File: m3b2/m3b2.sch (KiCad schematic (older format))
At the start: 41 parts, among them P6 MicroD-37Pins, Q1 MD3251, Q2 MD3251, U1 MC307, U10 MC308, U11 MC306, U12 MC308, U13 MC308, U14 MC308, U15 MC306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

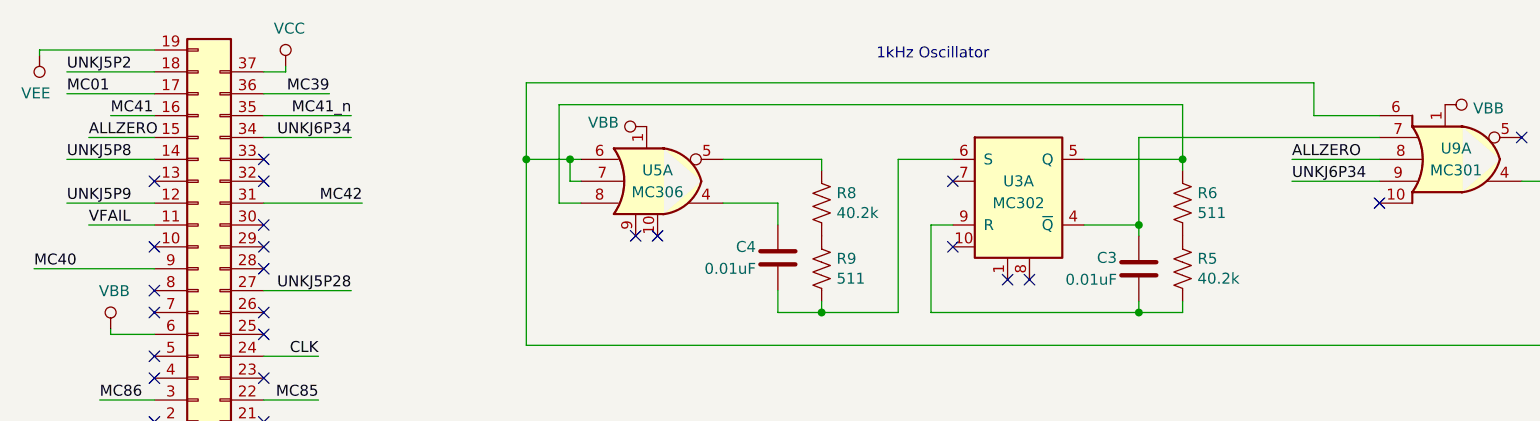
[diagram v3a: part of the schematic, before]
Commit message: Initial schematic for module 4, board 1, plus lots of associated net name updates. The shift register is done, but a lot of surrounding NOR logic still needs to be untangled.
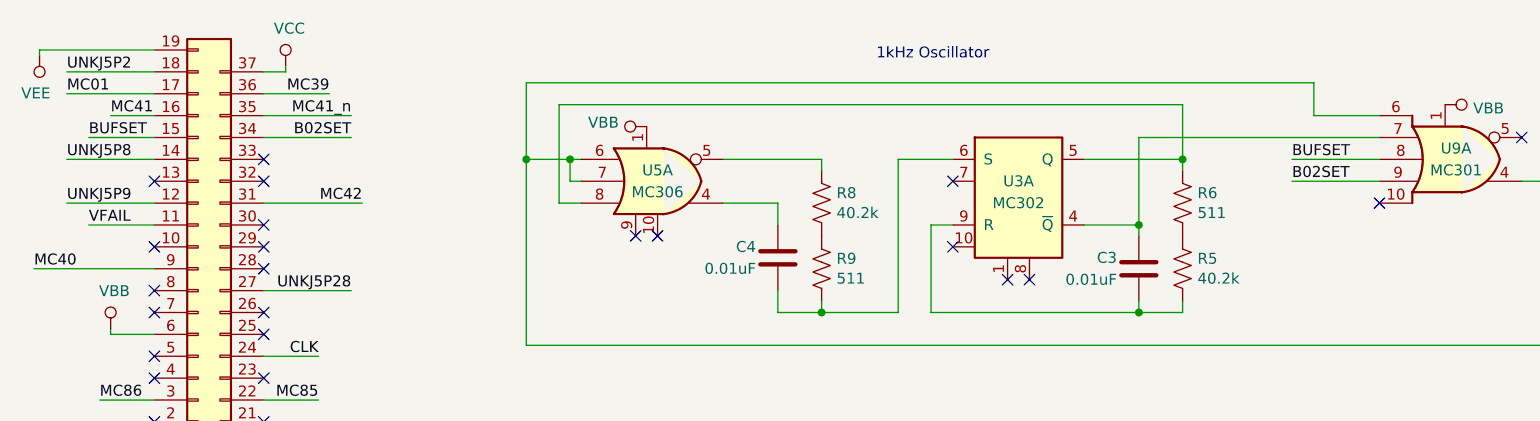
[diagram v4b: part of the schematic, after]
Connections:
- net ALLZERO renamed BUFSET
- net UNKJ6P34 renamed B02SET
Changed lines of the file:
@@
 	1200 1150 900  1150
 Text Label 900  1150 0    50   ~ 0
-ALLZERO
+BUFSET
 Wire Wire Line
 	1700 1850 2100 1850
@@
 	1700 1150 2100 1150
 Text Label 2100 1150 2    50   ~ 0
-UNKJ6P34
+B02SET
 Wire Wire Line
 	1700 1050 2100 1050
@@
 	6800 1250 6400 1250
 Text Label 6400 1250 0    50   ~ 0
-ALLZERO
+BUFSET
 Wire Wire Line
 	6800 1350 6400 1350
 Text Label 6400 1350 0    50   ~ 0
-UNKJ6P34
+B02SET
 Wire Wire Line
 	7450 1350 7700 1350

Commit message: Some work on reorganizing the module 3 schematics
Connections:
- net at U13.4 (~Q), U5.6, U5.7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: now also U10.1 (R), U14.1 (R), U4.1 (R), U6.1 (R)
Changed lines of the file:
@@
 	9050 6400 8350 6400
 Wire Wire Line
-	9050 2100 9050 6400
+	9050 2100 9050 3800
 $Comp
 L Device:R_US R12
@@
 Text Label 8450 9100 2    50   ~ 0
 MC42
+Wire Wire Line
+	4550 3800 9050 3800
+Connection ~ 4550 3800
+Connection ~ 9050 3800
+Wire Wire Line
+	9050 3800 9050 6400
 $EndSCHEMATC

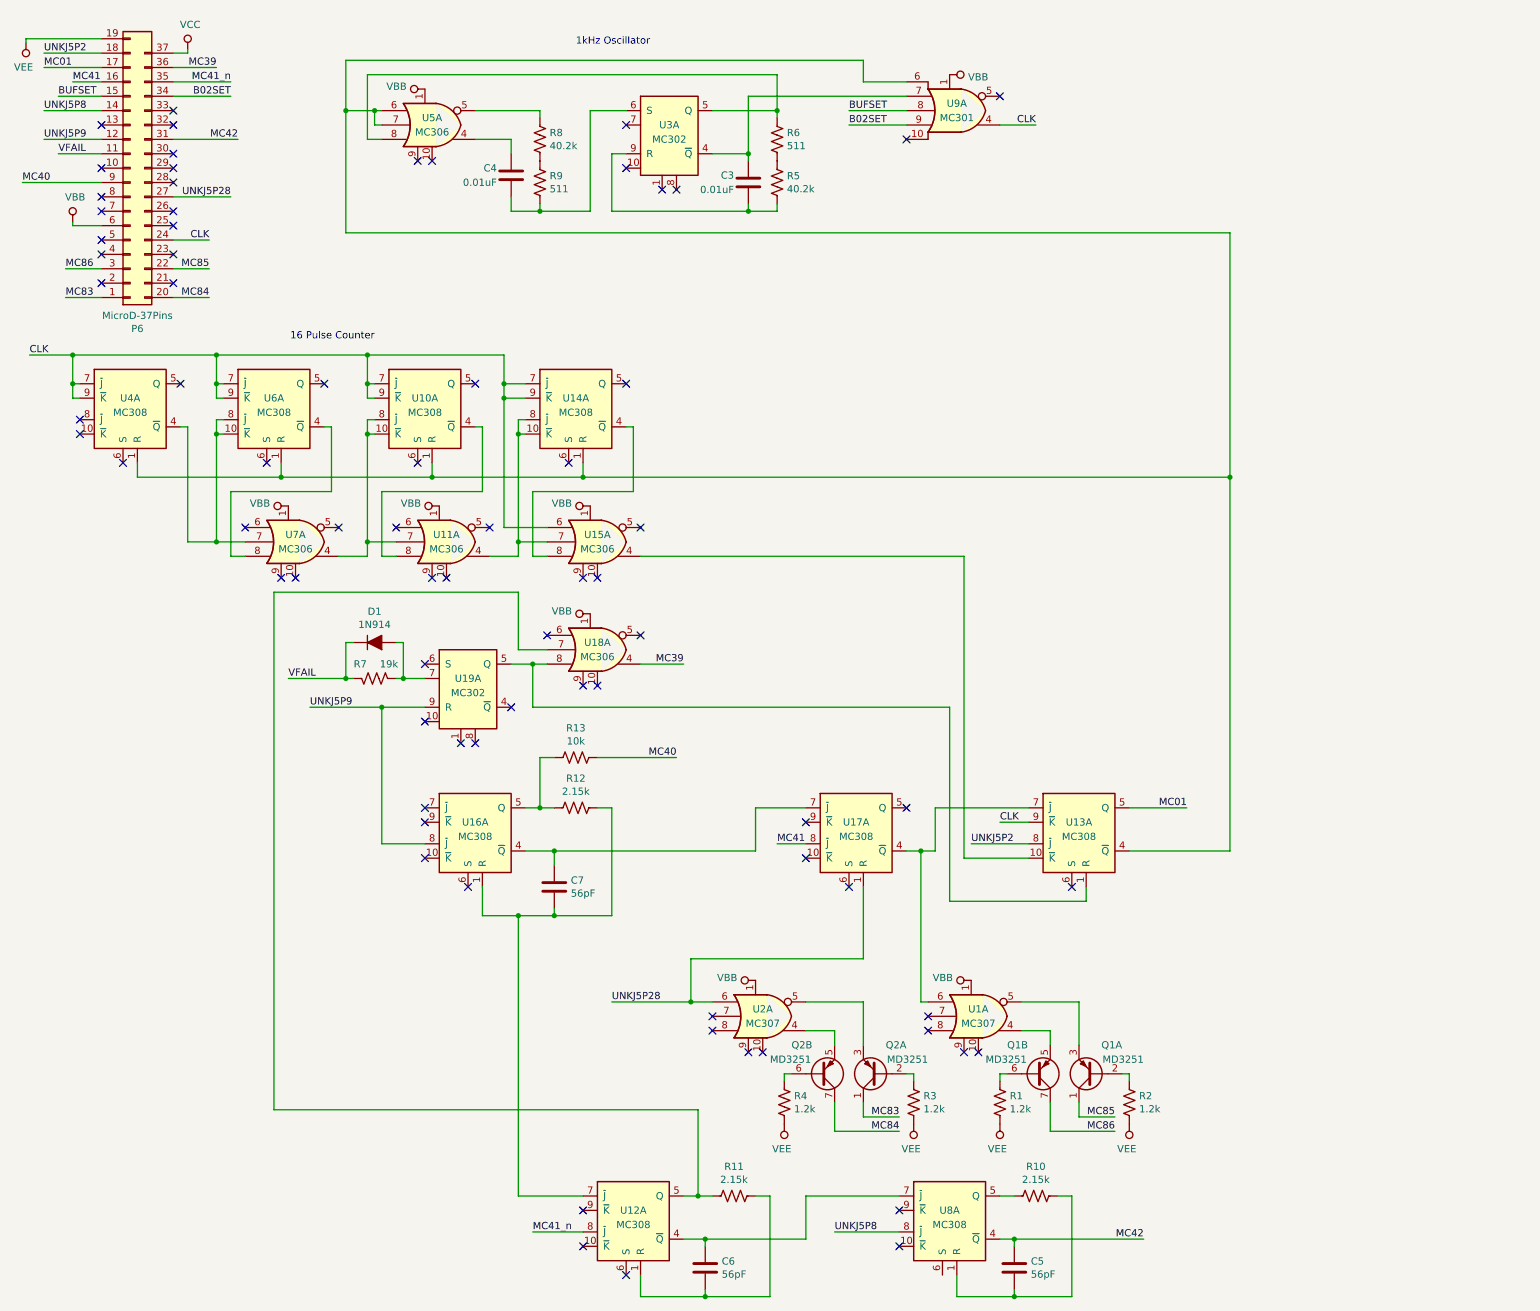
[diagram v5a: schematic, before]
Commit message: Finished untangling the module 3 schematics and gave every net a name
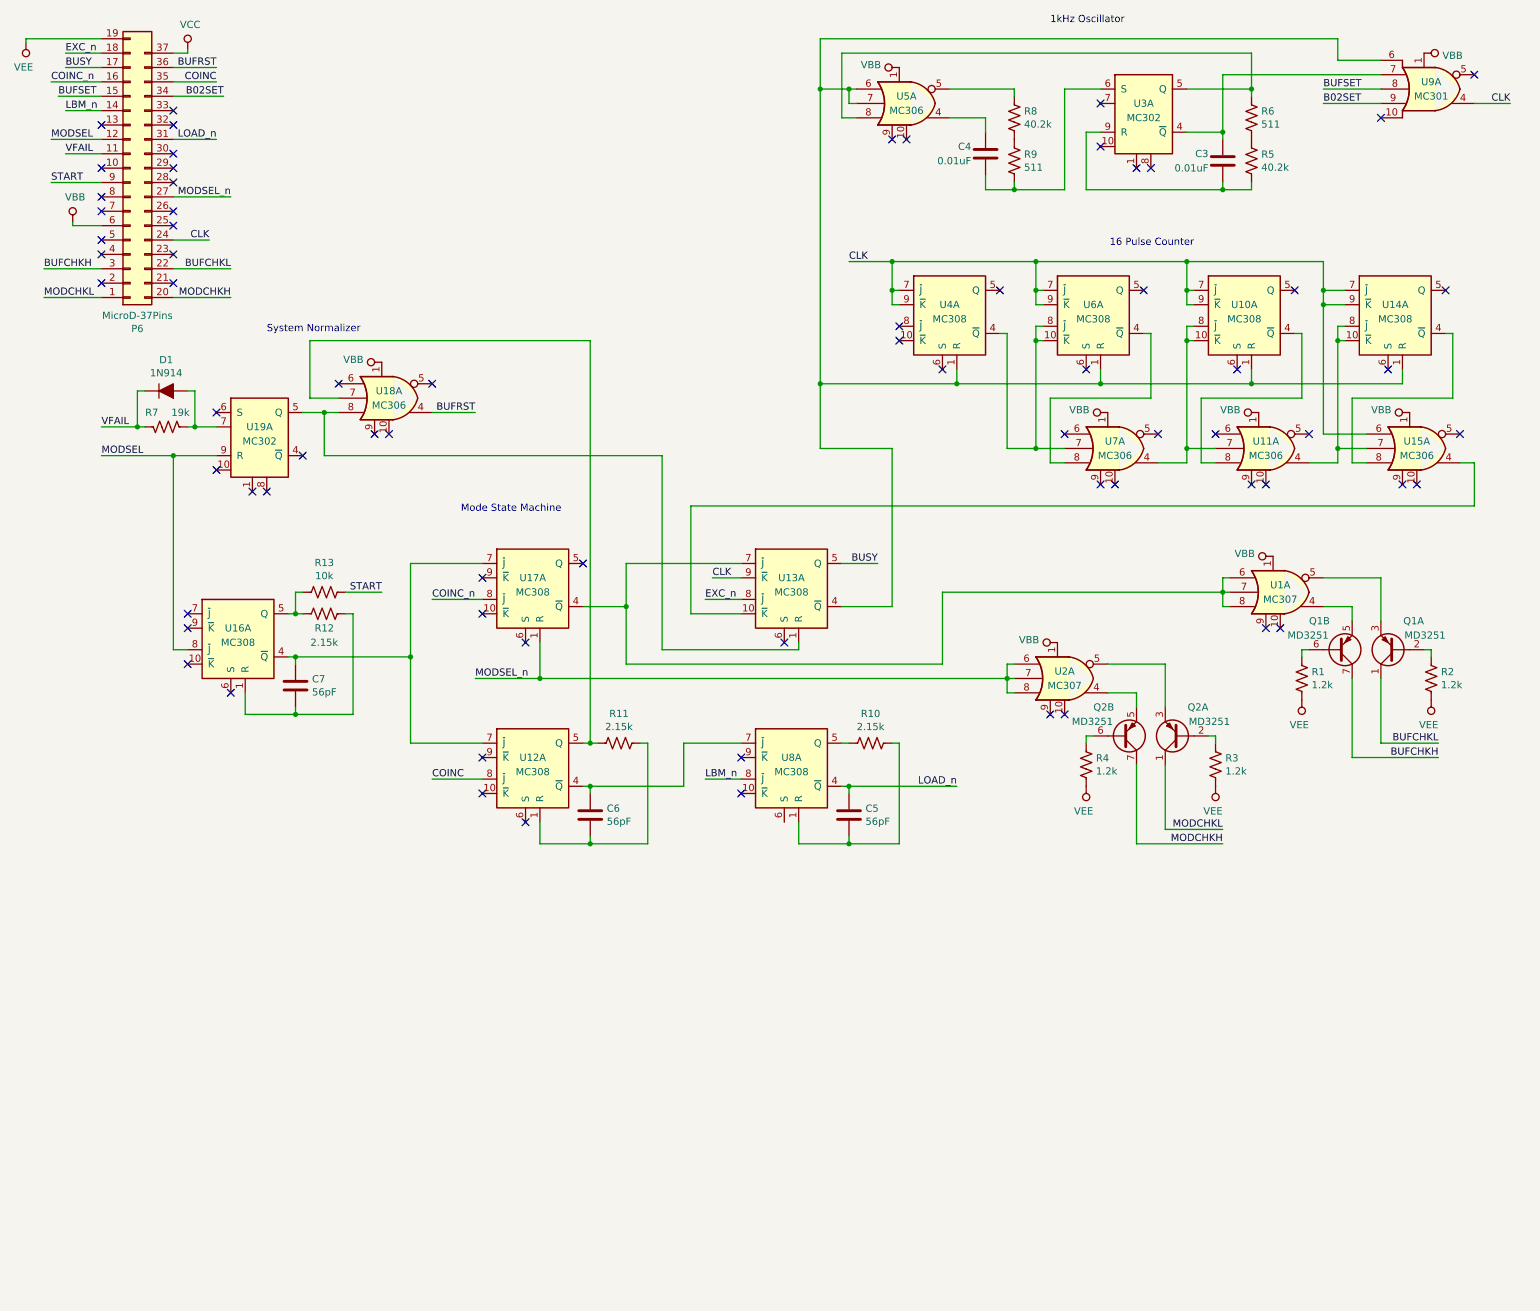
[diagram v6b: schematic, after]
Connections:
- net UNKJ5P28 is gone; now on net MODSEL_n: P6.27 (Pin_27), U17.1 (R), U2.6
- net at U1.6, U13.7 (~J), U17.4 (~Q): now also U1.7, U1.8
- net MODSEL_n: now reaches U2.7
- net MODSEL_n: now also U2.8
- net at C7.2, R12.1, U16.1 (R): no longer U12.7 (~J)
- net at C7.1, U16.4 (~Q), U17.7 (~J): now also U12.7 (~J)
- net MC01 renamed BUSY
- net MC39 renamed BUFRST
- net MC40 renamed START
- net MC41 renamed COINC_n
- net MC41_n renamed COINC
- net MC42 renamed LOAD_n
- net MC83 renamed MODCHKL
- net MC84 renamed MODCHKH
- net MC85 renamed BUFCHKL
- net MC86 renamed BUFCHKH
- net UNKJ5P2 renamed EXC_n
- net UNKJ5P8 renamed LBM_n
- net UNKJ5P9 renamed MODSEL
- no-connect marks 76 -> 72
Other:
- note added: "Mode State Machine"
- note added: "System Normalizer"
- moved on the sheet: C3, C4, C5, C6, C7, D1, Q1A, Q1B, Q2A, Q2B, R1, R10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

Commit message: Greatly cleaned up all of the schematics so far; everything passes DRC.
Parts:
- added C1, C2: 0.1uF, symbol Device:C
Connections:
- net VBB: now also C1.2
- net VCC: now also C1.1, C2.1
- net VEE: now also C2.2
- no-connect marks 72 -> 73
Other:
- note added: "Backplane Connections"
- note added: "Buffer Check"
- note added: "Mode Check"
- moved on the sheet: C3, C4, D1, R5, R6, R7, R8, R9, U10A, U11A, U14A, U15A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
